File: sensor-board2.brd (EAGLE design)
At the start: 79 parts, among them IC1 MCP3423, IC10_ADJ LD117AS12TR, IC1_VDD=7.5V MAX4194, IC2 MPXHZ6115A6U, IC3 MPX2010, IC4 MAG3110, IC5 MMA8652FC, IC6 FXAS21002C, IC7 RFM95, IC8 LM2731(X/Y), IC8_5V LD117AS12TR, IC9_3.3V LD117AS12TR, IC9_3.3V1 LD117AS12TR, J2 JP7, Q1 BSS123, Q2 BSS123, X1 SMA-142-0701-801/806

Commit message: cdn
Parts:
- removed L1: POWER_INDUCTOR_SMD, micrel:7X7X4
- added C15: 4u7/25V, rcl:SMC_D
- added C20: 270p, rcl:C0805
- added C21: krowka_10/25V, rcl:SMC_D
- added L2: POWER_INDUCTOR, miscrel:7X7X4
- added R15: 12k (zalecaja 13k3), resistor:R0805
- added R16: 100k, resistor:R0805
- added R17: 10k, resistor:R0805
- added R18: 50k, resistor:R0805
- Q1, Q2: value BSS123 -> AO3402; device transistor-small-signal:SOT23 -> TI:SOT23-3
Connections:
- new net N$19: C20.1, IC8.3, R15.1, R16.1
- new net N$20: C15.-, C21.-, IC8.2, R15.2
- new net N$23: C15.+, C20.2, D5.C, R16.2
- new net N$28: IC8.4, R18.1
- net GND: no longer IC8.2
- net N$17: now also L2.2; no longer L1.2
- net N$2: now also C21.+, L2.1, R18.2; no longer L1.1
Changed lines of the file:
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@@
 <element name="D4" library="diode" package="MELF-MLL41" value="" x="62.78" y="-53.41" rot="R90"/>
 <element name="J2" library="jumper" package="JP7" value="JP7" x="72.81" y="-67.06" rot="R90"/>
-<element name="Q1" library="transistor-small-signal" package="SOT23" value="BSS123" x="53.34" y="10.16"/>
-<element name="Q2" library="transistor-small-signal" package="SOT23" value="BSS123" x="53.34" y="2.54"/>
+<element name="Q1" library="TI" package="SOT23-3" value="AO3402" x="53.34" y="10.16"/>
+<element name="Q2" library="TI" package="SOT23-3" value="AO3402" x="53.34" y="2.54"/>
 <element name="R6" library="resistor" package="R0805" value="4k7" x="53.34" y="-5.08"/>
 <element name="R7" library="resistor" package="R0805" value="10k" x="53.34" y="-11.43"/>
@@
 <element name="R14" library="resistor" package="R0805" value="2k2" x="53.34" y="-36.83"/>
 <element name="IC8" library="TI" package="SOT23-5" value="LM2731(X/Y)" x="53.34" y="-87.63"/>
-<element name="L1" library="micrel" package="7X7X4" value="POWER_INDUCTOR_SMD" x="57.15" y="-96.52"/>
 <element name="D5" library="diode" package="MELF-MLL41" value="1N5819" x="55.88" y="-105.41"/>
+<element name="R15" library="resistor" package="R0805" value="12k (zalecaja 13k3)" x="53.34" y="-113.03"/>
+<element name="R16" library="resistor" package="R0805" value="100k" x="53.34" y="-119.38"/>
+<element name="R17" library="resistor" package="R0805" value="10k" x="53.34" y="-125.73"/>
+<element name="C15" library="rcl" package="SMC_D" value="4u7/25V" x="55.88" y="-151.13"/>
+<element name="C20" library="rcl" package="C0805" value="270p" x="53.34" y="-158.75"/>
+<element name="C21" library="rcl" package="SMC_D" value="krowka_10/25V" x="55.88" y="-166.37"/>
+<element name="R18" library="resistor" package="R0805" value="50k" x="53.34" y="-173.99"/>
+<element name="L2" library="miscrel" package="7X7X4" value="POWER_INDUCTOR" x="38.1" y="-170.18"/>
 </elements>
 <signals>
@@
 <contactref element="R7" pad="1"/>
 <contactref element="R14" pad="1"/>
-<contactref element="IC8" pad="2"/>
 <wire x1="99.1743" y1="42.40021875" x2="95.6374" y2="46.3725" width="0" layer="19" extent="1-1"/>
 <wire x1="89.8" y1="27.595" x2="89.9294" y2="22.926" width="0" layer="19" extent="1-1"/>
@@
 <wire x1="69.5589" y1="46.3405" x2="81.63315" y2="34.787" width="0" layer="19" extent="1-1"/>
 <wire x1="52.39" y1="-11.43" x2="69.5696" y2="-2.3447" width="0" layer="19" extent="1-1"/>
-<wire x1="53.34" y1="-88.93" x2="67.31" y2="-74.93" width="0" layer="19" extent="1-1"/>
 </signal>
 <signal name="N$1">
@@
 <signal name="N$2">
 <contactref element="IC8" pad="5"/>
-<contactref element="L1" pad="1"/>
-<wire x1="52.39" y1="-86.33" x2="57.15" y2="-94.195" width="0" layer="19" extent="1-1"/>
+<contactref element="C21" pad="+"/>
+<contactref element="R18" pad="2"/>
+<contactref element="L2" pad="1"/>
+<wire x1="52.73" y1="-166.37" x2="38.1" y2="-167.855" width="0" layer="19" extent="1-1"/>
+<wire x1="54.29" y1="-173.99" x2="52.73" y2="-166.37" width="0" layer="19" extent="1-1"/>
+<wire x1="52.39" y1="-86.33" x2="52.73" y2="-166.37" width="0" layer="19" extent="1-1"/>
 </signal>
 <signal name="N$17">
-<contactref element="L1" pad="2"/>
 <contactref element="IC8" pad="1"/>
 <contactref element="D5" pad="A"/>
-<wire x1="57.15" y1="-98.845" x2="58.505" y2="-105.41" width="0" layer="19" extent="1-1"/>
-<wire x1="52.39" y1="-88.93" x2="57.15" y2="-98.845" width="0" layer="19" extent="1-1"/>
+<contactref element="L2" pad="2"/>
+<wire x1="58.505" y1="-105.41" x2="38.1" y2="-172.505" width="0" layer="19" extent="1-1"/>
+<wire x1="52.39" y1="-88.93" x2="58.505" y2="-105.41" width="0" layer="19" extent="1-1"/>
+</signal>
+<signal name="N$19">
+<contactref element="IC8" pad="3"/>
+<contactref element="R15" pad="1"/>
+<contactref element="R16" pad="1"/>
+<contactref element="C20" pad="1"/>
+<wire x1="52.39" y1="-119.38" x2="52.39" y2="-158.75" width="0" layer="19" extent="1-1"/>
+<wire x1="52.39" y1="-113.03" x2="52.39" y2="-119.38" width="0" layer="19" extent="1-1"/>
+<wire x1="54.29" y1="-88.93" x2="52.39" y2="-113.03" width="0" layer="19" extent="1-1"/>
+</signal>
+<signal name="N$20">
+<contactref element="R15" pad="2"/>
+<contactref element="C15" pad="-"/>
+<contactref element="IC8" pad="2"/>
+<contactref element="C21" pad="-"/>
+<wire x1="59.03" y1="-151.13" x2="59.03" y2="-166.37" width="0" layer="19" extent="1-1"/>
+<wire x1="54.29" y1="-113.03" x2="59.03" y2="-151.13" width="0" layer="19" extent="1-1"/>
+<wire x1="53.34" y1="-88.93" x2="54.29" y2="-113.03" width="0" layer="19" extent="1-1"/>
+</signal>
+<signal name="N$23">
+<contactref element="C20" pad="2"/>
+<contactref element="C15" pad="+"/>
+<contactref element="R16" pad="2"/>
+<contactref element="D5" pad="C"/>
+<wire x1="52.73" y1="-151.13" x2="54.29" y2="-158.75" width="0" layer="19" extent="1-1"/>
+<wire x1="54.29" y1="-119.38" x2="52.73" y2="-151.13" width="0" layer="19" extent="1-1"/>
+<wire x1="53.255" y1="-105.41" x2="54.29" y2="-119.38" width="0" layer="19" extent="1-1"/>
+</signal>
+<signal name="N$28">
+<contactref element="IC8" pad="4"/>
+<contactref element="R18" pad="1"/>
+<wire x1="54.29" y1="-86.33" x2="52.39" y2="-173.99" width="0" layer="19" extent="1-1"/>
 </signal>
 </signals>

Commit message: IO discrete buffers
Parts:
- added IC10, IC9, Q11, Q12, Q13, Q14, Q15, Q16, Q3, Q4, Q5, Q6, Q7, Q8, Q9: (no value), TI:SOT23-3
- added IC11: 4504D, 45xx:SO16
- added R19: 82k, resistor:R0805
- added R20: 33k, resistor:R0805
- added R21, R22, R25, R26, R30, R32, R34, R36, R38, R40: 10k, resistor:R0805
- added R23: 2k2, resistor:R0805
- added R24, R27, R31, R33, R35, R37, R39, R41: 4k7, resistor:R0805
- added ZOLTY_TANTAL1: 22uF/10v, rcl:SMC_B
- IC1_VDD=7.5V: value MAX4194 -> (none)
- IC2: value MPXHZ6115A6U -> (none)
- IC3: value MPX2010 -> (none)
- IC4: value MAG3110 -> (none)
- IC5: value MMA8652FC -> (none)
- IC6: value FXAS21002C -> (none)
- IC7: value RFM95 -> (none)
- IC8: value LM2731(X/Y) -> (none)
- L2: value POWER_INDUCTOR -> (none)
- Q1, Q2: value AO3402 -> (none)
- R7: value 10k -> 4k7
- moved R6 307.8 mm to (36.8, -312.4)
- moved R7 307.8 mm to (36.8, -318.8)
- moved R17 200.1 mm to (36.8, -325.1)
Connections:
- removed net REF3V3: Q1.1, Q2.1, R6.1, R7.2
- new net INT1_B: JP3.2, Q12.3, R32.1
- new net INT1_XX_B: JP4.1, Q16.3, R40.1
- new net INT1_X_B: JP4.2, Q15.3, R38.1
- new net INT2_B: JP3.1, Q13.3, R34.1
- new net INT2_X_B: JP4.3, Q14.3, R36.1
- new net MISO_B: Q3.3
- new net MOSI_B: Q4.3
- new net N$21: IC9.2, R19.2, R20.1
- new net N$22: IC10.2, IC9.1, R21.1, R22.2, ZOLTY_TANTAL1.-
- new net N$24: Q11.2, R31.1
- new net N$27: IC10.3
- new net N$29: IC10.1, R26.1
- new net N$30: R20.2, R21.2, R26.2, ZOLTY_TANTAL1.+
- new net N$33: Q12.2, R33.1
- new net N$35: Q13.2, R35.1
- new net N$37: Q14.2, R37.1
- new net N$39: Q15.2, R39.1
- new net N$41: Q16.2, R41.1
- new net NSS_B: Q6.3
- new net RESET_B: Q7.3
- new net RST_B_B: JP3.3, Q11.3, R30.1
- new net SCK_B: Q5.3
- new net SCL2_B: JP2.3, Q8.3, R17.1
- new net SDA2_B: JP2.2, Q9.3, R25.1
- new net VCC: IC11.1
- new net VDD: IC11.16
- new net V_LOC: Q3.1, Q4.1, Q5.1, Q6.1, Q7.1, R23.1
- net +3V3: now also R23.2
- net +5V: now also Q1.1, Q2.1, R17.2, R25.2, R30.2, R32.2, R34.2, R36.2, R38.2, R40.2, R7.2
- net GND: now also IC11.8; no longer R7.1
- net INT1: no longer JP3.2
- net INT1_X: no longer JP4.2
- net INT1_XX: no longer JP4.1
- net INT2: no longer JP3.1
- net INT2_X: no longer JP4.3
- net MISO: now also Q3.2
- net MOSI: now also Q4.2; no longer J2.5
- net NSS: now also Q6.2; no longer J2.3
- net RESET: now also Q7.2; no longer J2.2
- net RST_B: no longer JP3.3
- net SCK: now also Q5.2; no longer J2.4
- net SCL-R: now also R7.1
- net SCL2: now also Q8.2, R24.1; no longer JP2.3
- net SDA-R: now also R6.1
- net SDA2: now also Q9.2, R27.1; no longer JP2.2
- net VCCIO: now also Q11.1, Q12.1, Q13.1, Q14.1, Q15.1, Q16.1, Q8.1, Q9.1, R24.2, R27.2, R31.2, R33.2, R35.2, R37.2, R39.2, R41.2
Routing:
- net RST_B: track 26.7 -> 11.2 mm
- net INT1: track 13.5 -> 3.59 mm
- net SCL2: track 14.5 -> 9.19 mm
- net SDA2: track 26.1 -> 22.8 mm
- net INT2_X: track 7.47 -> 4.45 mm
- net INT2: track 5.51 -> 2.68 mm
- net NSS: track 5.33 -> 3.60 mm
- net RESET: track 5.56 -> 3.82 mm
- net INT1_X: track 24.7 -> 23.1 mm
- net INT1_XX: track 34.5 -> 32.8 mm
- net SCK: track 5.12 -> 3.78 mm

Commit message: overvoltage protection
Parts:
- removed IC10: (no value), TI:SOT23-3
- removed IC11: 4504D, 45xx:SO16
- removed R26: 10k, resistor:R0805
- removed ZOLTY_TANTAL1: 22uF/10v, rcl:SMC_B
- added C22: 330uF/6V2, rcl:SMC_D
- added C23: 100n, rcl:C0805
- added D6, D7: (no value), diode:MELF-MLL41
- added IC9_3.3V2: LD117AS12TR, v-reg:SOT223
- added LED4: (no value), eagle-ltspice:LED_1206
- added Q10, Q17: IRF540, transistor-power:TO220BV
- added Q18: BC807-16LT1SMD, transistor-pnp:SOT23-BEC
- added R28: 27k, resistor:R0805
- added R29: 15k, resistor:R0805
- added R42: 3k3, resistor:R0805
- added T1: BC847, transistor:SOT23
- R21: value 10k -> 1k5
- R22: value 10k -> 330k
- moved R21 325.3 mm to (26.7, -535.9)
- moved R22 272.0 mm to (26.7, -488.9)
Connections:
- removed net VCC: IC11.1
- removed net VDD: IC11.16
- new net N$26: Q17.G, Q18.C, R42.2
- new net N$31: IC9_3.3V2.1
- new net N$32: C23.2
- new net N$34: IC9.1, R29.1
- new net N$38: R42.1
- new net N$42: Q10.G, Q17.D, R28.2
- net GND: no longer IC11.8
- net N$21: now also C23.1
- net N$22: now also IC9_3.3V2.2, IC9_3.3V2.4, Q10.D; no longer IC10.2, IC9.1, R21.1, R22.2, ZOLTY_TANTAL1.-
- net N$27: now also Q18.B, R22.1, R29.2; no longer IC10.3
- net N$29: now also IC9_3.3V2.3, Q18.E, R22.2, R28.1; no longer IC10.1, R26.1
- net N$30: now also Q10.S; no longer R21.2, R26.2, ZOLTY_TANTAL1.+

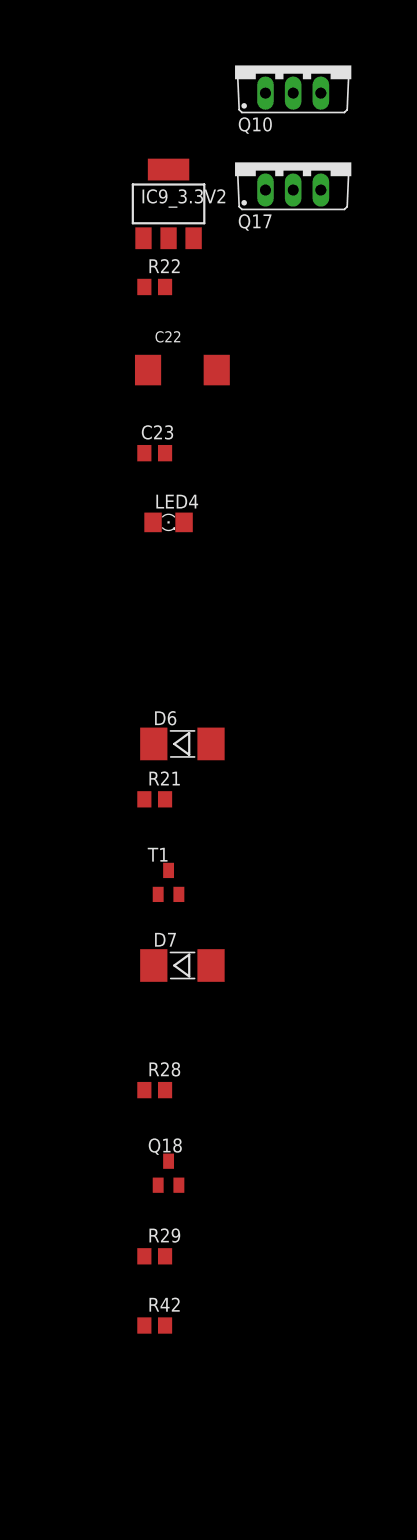
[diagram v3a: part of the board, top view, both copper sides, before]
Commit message: overvoltage protection fix
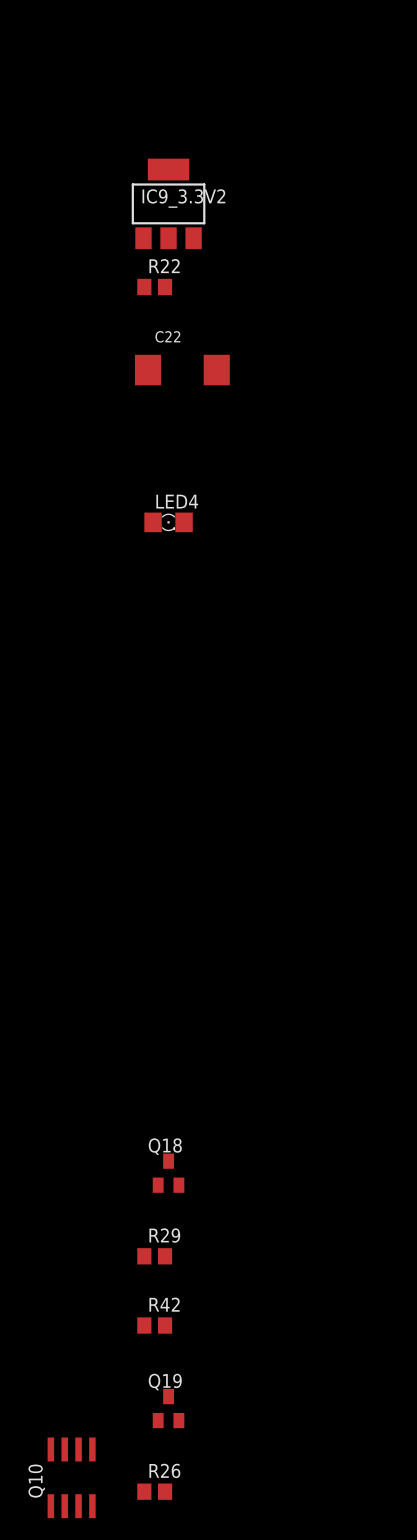
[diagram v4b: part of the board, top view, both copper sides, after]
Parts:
- removed C23: 100n, rcl:C0805
- removed D6, D7: (no value), diode:MELF-MLL41
- removed Q17: IRF540, transistor-power:TO220BV
- removed R21: 1k5, resistor:R0805
- removed R28: 27k, resistor:R0805
- removed T1: BC847, transistor:SOT23
- added Q19: IRLML2060, miscrel:SOT23-3
- added R26: 1k, resistor:R0805
- IC2: value (none) -> MPXHZ6115A6U
- IC3: value (none) -> MPX2010
- IC4: value (none) -> MAG3110
- IC5: value (none) -> MMA8652FC
- IC6: value (none) -> FXAS21002C
- IC7: value (none) -> RFM95
- IC8: value (none) -> LM2731(X/Y)
- IC9: value (none) -> TLV431 (1.24VREF)
- Q10: value IRF540 -> (none); device transistor-power:TO220BV -> transistor-power:SO-08
- R19: value 82k -> 100k
- R20: value 33k -> 180k
- R22: value 330k -> 1M
- R29: value 15k -> 100k
- moved Q10 131.1 mm to (19.1, -598.2)
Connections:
- removed net N$26: Q17.G, Q18.C, R42.2
- removed net N$42: Q10.G, Q17.D, R28.2
- new net N$36: Q19.2
- new net N$40: Q19.3, R26.2
- new net S3V3_FAULT: Q10.4, Q18.C, Q19.1, R42.2
- net N$21: no longer C23.1
- net N$22: now also Q10.1, Q10.2, Q10.3; no longer Q10.D
- net N$27: no longer R22.1
- net N$29: now also LED4.A; no longer R28.1
- net N$30: now also Q10.5, Q10.6, Q10.7, Q10.8; no longer Q10.S
- net N$32: now also LED4.C, R26.1; no longer C23.2
- net N$34: now also R22.1

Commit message: 12/6/5 voltages added
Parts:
- removed D5: 1N5819, diode:MELF-MLL41
- removed IC9_3.3V2: LD117AS12TR, v-reg:SOT223
- removed L2: (no value), miscrel:7X7X4
- added C23, C24: 1u/50V, rcl:C1206
- added C25: 560p/50V, rcl:C1206
- added C26, C29: 4u7/16V, resistor:C1206
- added C28, C30: 22u/25V, rcl:C/6032-28R
- added C31: 470p/50V, rcl:C1206
- added D6: 3v3, diode:SOD80C
- added D7: 1N5819, diode:MELF-MLL41
- added D8, D9: 4001, diode:DO-214AC
- added IC10: LM2731(X/Y), TI:SOT23-5
- added IC11: TLV702, TI:SOT23-5
- added IC12: TC1044SEOA, TI:SOIC8
- added IC13: MIC5209, TI:SOIC8
- added IC15: LM393D, linear:SO08
- added L1: 10uH, miscrel:7X7X4
- added Q17: DMP3130L, miscrel:SOT23-3
- added R21, R48: 1M, resistor:R0805
- added R28: 12k, resistor:R0805
- added R43, R45: 47k, resistor:R0805
- added R44, R47: 56k, resistor:R0805
- added R46: 330k, resistor:R0805
- added R51: 100k, resistor:R0805
- added R52: 15k, resistor:R0805
- C15: value 4u7/25V -> 22u/25V; device rcl:SMC_D -> rcl:C/6032-28R
- C20: value 270p -> 22u/25V; device rcl:C0805 -> rcl:C/6032-28R
- C21: value krowka_10/25V -> 470p/50V; device rcl:SMC_D -> rcl:C1206
- C22: value 330uF/6V2 -> 1u/50V; device rcl:SMC_D -> rcl:C1206
- IC8: value LM2731(X/Y) -> MIC5209; device TI:SOT23-5 -> TI:SOIC8
- LED4: value (none) -> FAULT IND RED
- Q10: value (none) -> DMP3130L; device transistor-power:SO-08 -> miscrel:SOT23-3
- R15: value 12k (zalecaja 13k3) -> 33k
- R18: value 50k -> 56k
- moved IC8 676.6 mm to (-1.27, -762.0)
- moved R15 671.6 mm to (-2.54, -782.3)
- moved R16 658.3 mm to (6.35, -776.0)
- moved R18 633.7 mm to (-2.54, -805.2)
- moved C20 633.5 mm to (-1.27, -789.9)
- moved C21 606.1 mm to (-2.54, -769.6)
- moved C15 603.4 mm to (-1.27, -751.8)
- moved C22 243.4 mm to (-2.54, -737.9)
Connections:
- removed net S3V3_FAULT: Q10.4, Q18.C, Q19.1, R42.2
- new net -CAP: IC12.4
- new net 3V3_FOR_LORA: Q10.3, R20.2
- new net BOOST_SENS_A+: C31.2, IC13.4, R45.1, R46.1
- new net BOOST_SENS_A-: R51.1, R52.2
- new net LOW_SHDN_6V: IC10.4, R44.1
- new net N$26: IC11.3
- new net N$42: IC15.3
- new net N$43: C28.+, D9.C, IC13.2, R18.1
- new net N$44: C22.1, IC13.3, R46.2, R51.2
- new net N$45: IC15.2
- new net N$46: IC13.1, R18.2
- new net POWER_FAULT_3V3_PLOGIC_CMOS: D6.C, R21.1
- new net PUMP_HI_TO_SHDN: Q17.1
- new net REHREH: Q10.1, Q18.C, Q19.1, R21.2, R42.2
- new net TO_BATT: C24.1, IC11.1, LED4.A, Q18.E, R22.2
- net GND: now also C15.-, C20.-, C21.1, C22.2, C23.1, C24.2, C26.2, C28.-, C31.1, D6.A, IC10.2, IC11.2, IC12.3, IC12.5, IC13.5, IC13.6, IC13.7, IC13.8, IC15.4, IC8.5, IC8.6, IC8.7, IC8.8, IC9.3, Q19.2, R15.2, R19.1, R28.2, R42.1, R45.2, R52.1
- net N$17: now also C20.+, IC8.3, R16.2; no longer D5.A, IC8.1, L2.2
- net N$19: now also IC8.1, R47.2; no longer C20.1, IC8.3, R15.1, R16.1
- net N$2: now also C21.2, IC8.4, R15.1, R16.1; no longer C21.+, IC8.5, L2.1, R18.2
- net N$20: now also C15.+, C25.1, D7.C, Q17.2, R43.2, R47.1; no longer C15.-, C21.-, R15.2
- net N$21: now also IC9.1; no longer IC9.2
- net N$22: now also C23.2, IC11.5; no longer IC9_3.3V2.2, IC9_3.3V2.4, Q10.1, Q10.3
- net N$23: now also D8.A, IC12.8, IC15.8, Q17.3, R48.2; no longer C15.+, C20.2, D5.C, R16.2
- net N$28: now also C29.2, D8.C, D9.A; no longer IC8.4, R18.1
- net N$29: now also C26.1, IC10.5, L1.1, R44.2; no longer IC9_3.3V2.3, LED4.A, Q18.E, R22.2
- net N$30: now also D7.A, IC10.1, L1.2; no longer Q10.5, Q10.6, Q10.7, Q10.8, R20.2
- net N$31: now also C25.2, IC10.3, R28.1, R43.1; no longer IC9_3.3V2.1
- net N$34: now also IC9.2; no longer IC9.1
- net N$36: now also C29.1, IC12.2; no longer Q19.2
- net N$38: now also IC12.1, IC15.1, R48.1; no longer R42.1

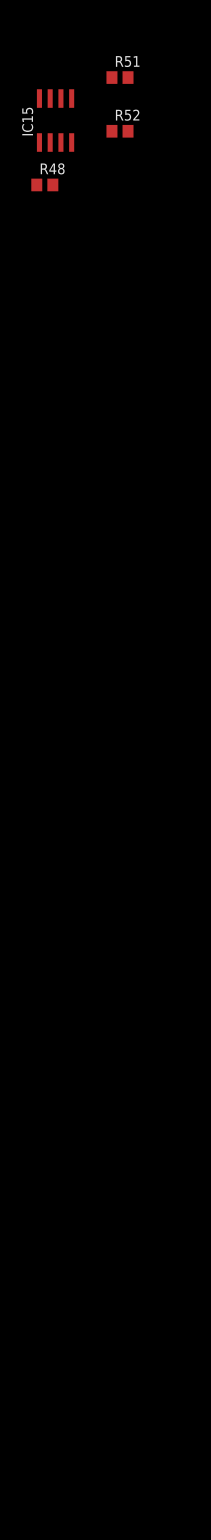
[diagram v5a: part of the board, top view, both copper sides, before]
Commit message: 12-10 care with the BOOST mode
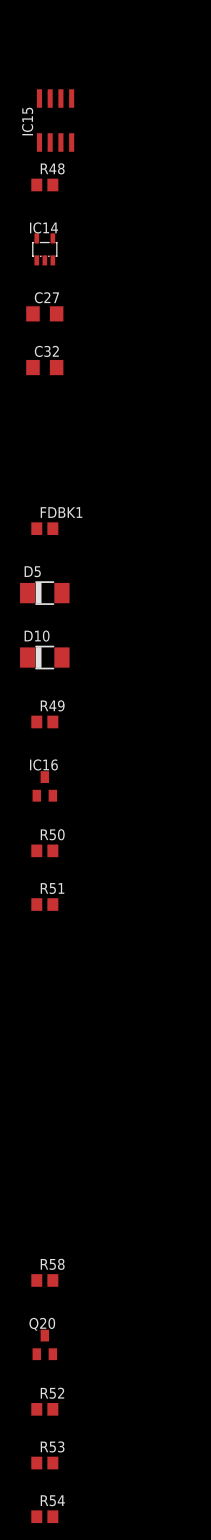
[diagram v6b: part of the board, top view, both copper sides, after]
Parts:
- added C27, C32: 1u/50V, rcl:C1206
- added D10, D5: 4001, diode:DO-214AC
- added FDBK1: 680k, resistor:R0805
- added IC14: TLV702, TI:SOT23-5
- added IC16: TLV431, TI:SOT23-3
- added Q20: DMP3130L, miscrel:SOT23-3
- added R49: 390k, resistor:R0805
- added R50: 12k, resistor:R0805
- added R53: 22k, resistor:R0805
- added R54: 39k, resistor:R0805
- added R58: 68k, resistor:R0805
- D6: value 3v3 -> 3V3
- R19, R29: value 100k -> 22k
- R20: value 180k -> 39k
- R21: value 1M -> 22k
- R22: value 1M -> 560k
- R48: value 1M -> 10k
- R51: value 100k -> 10k
- R52: value 15k -> 39k
- moved R52 151.4 mm to (-11.4, -1010.9)
- moved R51 98.2 mm to (-11.4, -951.2)
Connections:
- removed net BOOST_SENS_A+: C31.2, IC13.4, R45.1, R46.1
- removed net BOOST_SENS_A-: R51.1, R52.2
- removed net N$21: IC9.1, R19.2, R20.1
- new net BOOST_SENS_1.242: C31.2, IC13.4, IC15.3, R45.1, R46.1
- new net N$47: C27.2, IC14.5, Q20.2
- new net N$48: IC14.3
- new net N$49: Q20.3, R52.2
- new net N$50: FDBK1.1, IC9.1, R19.2, R20.1
- new net REF(1.24): IC16.1, IC16.2, R50.1, R51.1
- net GND: now also C27.1, C32.2, IC14.2, IC16.3, R53.1, R58.2; no longer R52.1
- net N$17: now also D10.A
- net N$20: now also D10.C; no longer Q17.2
- net N$23: now also R50.2
- net N$38: now also R49.2
- net N$42: now also R52.1, R53.2; no longer IC15.3
- net N$43: now also D5.C
- net N$44: now also D5.A; no longer R51.2
- net N$45: now also R49.1, R51.2, R58.1; no longer IC15.2
- net REHREH: now also FDBK1.2
- net TO_BATT: now also C32.1, IC14.1

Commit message: All voltages protected
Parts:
- removed C30: 22u/25V, rcl:C/6032-28R
- removed Q20: DMP3130L, miscrel:SOT23-3
- removed R52, R54: 39k, resistor:R0805
- removed R53: 22k, resistor:R0805
- added D11, D12: 3V3, diode:SOD80C
- added FDBK2: 680k, resistor:R0805
- added IC17: TLV431 (1.24VREF), TI:SOT23-3
- added LED5: FAULT IND RED, eagle-ltspice:LED_1206
- added Q21, Q24: DMP3130L, miscrel:SOT23-3
- added Q22: BC807-16LT1SMD, transistor-pnp:SOT23-BEC
- added Q23: IRLML2060, miscrel:SOT23-3
- added R55, R57: 10k, resistor:R0805
- added R56: 33k, resistor:R0805
- added R59, R61, R64, R67: 22k, resistor:R0805
- added R60: 910k, resistor:R0805
- added R62: 39k, resistor:R0805
- added R63: 560k, resistor:R0805
- added R65: 3k3, resistor:R0805
- added R66: 1k, resistor:R0805
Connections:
- net POWER_FAULT_3V3_PLOGIC_CMOS renamed POWER_FAULT_3V3_LORA_PLOGIC_CMOS
- removed net N$42: R52.1, R53.2
- removed net N$47: C27.2, IC14.5, Q20.2
- removed net N$49: Q20.3, R52.2
- new net 3V3_FOR_IMU: Q24.3, R62.2
- new net N$21: IC15.7, Q21.1, R55.1, R59.1, R60.2
- new net N$51: Q21.3, R56.1
- new net N$52: Q22.B, R64.2
- new net N$53: IC17.2, R63.1, R64.1
- new net N$54: LED5.C, R66.1
- new net N$55: Q23.3, R66.2
- new net N$56: C27.2, IC14.5, Q24.2
- new net N$57: FDBK2.1, IC17.1, R61.2, R62.1
- new net POWER_FAULT_3V3_IMU_CMOS_PLOGIC: D12.C, R67.1
- new net POWER_FAULT_5V_CPU_CMOS_PLOGIC: D11.C, R59.2
- new net REHREH1: FDBK2.2, Q22.C, Q23.1, Q24.1, R65.2, R67.2
- new net TO_BATT1: C32.1, IC14.1, LED5.A, Q22.E, R63.2
- net GND: now also D11.A, D12.A, IC17.3, Q23.2, R57.2, R61.1, R65.1; no longer R53.1
- net N$17: now also Q21.2, R55.2
- net N$29: now also IC15.6, R56.2, R57.1, R60.1; no longer C26.1, IC10.5, L1.1, R44.2
- net REF(1.24): now also IC15.5
- net TO_BATT: now also C26.1, IC10.5, L1.1, R44.2; no longer C32.1, IC14.1
